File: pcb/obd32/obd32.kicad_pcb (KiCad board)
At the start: 2 copper layers, 43.2 x 43.2 mm, 36 parts, among them J1 USB_C_Receptacle_USB2.0, J2 Micro_SD_Card, J3 Conn_02x08_Top_Bottom, J4 USB_A, U1 LMR33630ADDA, U2 CP2102N-A01-GQFN24, U3 AP1117-33, U4 ESP32-WROOM-32, U5 SiP32431DR3, U6 MCP2562-E-MF

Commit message: Maybe version of board
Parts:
- removed C7, C8: 22µF, Capacitor_SMD:C_0805_2012Metric
- added C15: 10nF, Capacitor_SMD:C_0201_0603Metric, B.Cu at (236.2, 73.7)
- added C16: 0.47µF, Capacitor_SMD:C_0201_0603Metric, B.Cu at (236.7, 74.4)
- added C17: 0.1µF, Capacitor_SMD:C_0201_0603Metric, B.Cu at (238.8, 74.4)
- added C18: 0.1µF, Capacitor_SMD:C_0201_0603Metric, B.Cu at (229.6, 83.8)
- added D3: LED, LED_SMD:LED_0402_1005Metric, F.Cu at (221.0, 91.2)
- added D4: LED, LED_SMD:LED_0402_1005Metric, F.Cu at (223.3, 91.2)
- added D5: LED, LED_SMD:LED_0402_1005Metric, F.Cu at (225.6, 91.2)
- added J5: Conn_01x04_Female, Connector_PinSocket_2.54mm:PinSocket_1x04_P2.54mm_Vertical_SMD_Pin1Left, F.Cu at (199.9, 80.5)
- added R10: 4K7, Resistor_SMD:R_0201_0603Metric, F.Cu at (236.2, 90.4)
- added R11: 4K7, Resistor_SMD:R_0201_0603Metric, F.Cu at (237.5, 90.4)
- added R12: 65R, Resistor_SMD:R_0201_0603Metric, F.Cu at (222.5, 90.2)
- added R13: 65R, Resistor_SMD:R_0201_0603Metric, F.Cu at (224.0, 90.2)
- added R14: 5R, Resistor_SMD:R_0201_0603Metric, F.Cu at (225.6, 90.2)
- added SW1: SW_Push, Button_Switch_SMD:SW_SPST_B3U-3000P-B, F.Cu at (198.4, 64.8)
- added SW2: SW_Push, Button_Switch_SMD:SW_SPST_B3U-3000P-B, F.Cu at (198.4, 69.8)
- added U7: LPS25HB, Package_LGA:ST_HLGA-10_2.5x2.5mm_P0.6mm_LayoutBorder3x2y, B.Cu at (231.6, 84.1)
- C11, C12: value 100nF -> 0.1µF; footprint Capacitor_SMD:C_0805_2012Metric -> Capacitor_SMD:C_0201_0603Metric; moved to B.Cu
- C13, C14, C4: value 100nF -> 0.1µF; footprint Capacitor_SMD:C_0805_2012Metric -> Capacitor_SMD:C_0201_0603Metric
- C3: footprint Capacitor_SMD:C_0805_2012Metric -> Capacitor_SMD:C_0402_1005Metric
- C9: footprint Capacitor_SMD:C_0805_2012Metric -> Capacitor_SMD:C_0603_1608Metric
- J1: value USB_C_Receptacle_USB2.0 -> Conn_01x04_Male; footprint Connector_USB:USB_C_Receptacle_HRO_TYPE-C-31-M-12 -> Connector_Molex:Molex_PicoBlade_53048-0410_1x04_P1.25mm_Horizontal
- J3: value Conn_02x08_Top_Bottom -> OBD2; footprint Connector_PinHeader_2.54mm:PinHeader_2x08_P2.54mm_Vertical -> OBD2:OBD2
- J4: value USB_A -> 67329-8040; footprint Connector_USB:USB_A_Molex_105057_Vertical -> 67329-8040:673298040
- L1: value 8µH -> 2.2µH; footprint Inductor_SMD:L_Coilcraft_XxL4040 -> TDK_SPM5030:TDK_SPM5030
- R1, R2, R3, R4, R9: footprint Resistor_SMD:R_0603_1608Metric -> Resistor_SMD:R_0201_0603Metric
- R5, R6: value 5K1 -> 100K; footprint Resistor_SMD:R_0603_1608Metric -> Resistor_SMD:R_0201_0603Metric
- R7, R8: footprint Resistor_SMD:R_0603_1608Metric -> Resistor_SMD:R_0201_0603Metric; moved to F.Cu
- U1: value LMR33630ADDA -> LMR33630BDDA
- U2: value CP2102N-A01-GQFN24 -> ICM-20689; footprint Package_DFN_QFN:QFN-24-1EP_4x4mm_P0.5mm_EP2.6x2.6mm -> ICM-20689:QFN50P400X400X95-25N-D; moved to B.Cu
- U5: moved to B.Cu
- moved R5 38.9 mm to (237.2, 69.8), turned to 0 degrees
- moved J4 35.8 mm to (199.0, 103.6), turned to 90 degrees
- moved R6 35.2 mm to (226.8, 69.6), turned to 0 degrees
- moved J3 32.6 mm to (235.7, 64.1), turned to 180 degrees
- moved U2 32.3 mm to (236.5, 77.5)
- moved C12 24.0 mm to (209.8, 107.7)
- moved U5 21.3 mm to (209.4, 105.7), turned to 90 degrees
- moved R8 20.8 mm to (215.4, 73.8), turned to 270 degrees
- moved C11 19.6 mm to (209.0, 103.6)
- moved R7 17.7 mm to (215.4, 72.2), turned to 270 degrees
- moved C10 16.9 mm to (207.6, 90.4)
- moved C9 16.9 mm to (207.6, 86.6)
- moved U3 16.9 mm to (202.0, 88.5)
- moved C1 15.6 mm to (213.9, 73.2), turned to 270 degrees
- moved R1 14.1 mm to (207.8, 70.4), turned to 180 degrees
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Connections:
- J2 pad 9: Earth -> GND
- R5 pad 1: GND -> ESP32_EN
- R5 pad 2: Net-(J1-PadA5) -> +3V3
- R6 pad 1: Net-(J1-PadB5) -> ESP32_MISC
- R6 pad 2: GND -> +3V3
- U2 pad 10: (no net) -> Net-(C16-Pad2)
- U2 pad 12: (no net) -> IMU_INT
- U2 pad 13: (no net) -> +3V3
- U2 pad 2: GND -> (no net)
- U2 pad 20: UART_TX -> (no net)
- U2 pad 21: UART_RX -> (no net)
- U2 pad 22: (no net) -> +3V3
- U2 pad 23: (no net) -> I2C0_SCL
- U2 pad 24: (no net) -> I2C0_SDA
- U2 pad 3: USB_D+ -> (no net)
- U2 pad 4: USB_D- -> (no net)
- U2 pad 7: +5VA -> (no net)
- U2 pad 8: +5VA -> +3V3
- U2 pad 9: (no net) -> GND
- U4 pad 11: (no net) -> ESP32_MISC
- U4 pad 12: (no net) -> CAN_SHDN
- U4 pad 13: (no net) -> CAN_RX
- U4 pad 14: (no net) -> CAN_TX
- U4 pad 23: (no net) -> GPS_RX
- U4 pad 24: (no net) -> GPS_TX
- U4 pad 26: CAN_TX -> LED_R
- U4 pad 27: CAN_SHDN -> LED_G
- U4 pad 28: (no net) -> LED_B
- U4 pad 29: CAN_RX -> (no net)
- U4 pad 3: +3V3 -> ESP32_EN
- U4 pad 30: (no net) -> USB_EN
- U4 pad 31: (no net) -> BARO_INT
- U4 pad 36: (no net) -> I2C0_SDA
- U4 pad 37: (no net) -> I2C0_SCL
- U4 pad 7: USB_EN -> IMU_INT
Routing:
- net GND: track 203.4 -> 351.0 mm, vias 2 -> 8
- net +3V3: track 71.9 -> 171.7 mm, vias 3 -> 5
- net Earth: track 78.5 -> 0.00 mm
- net +BATT: track 61.8 -> 13.7 mm
- net ESP32_EN: track 0.00 -> 45.5 mm
- net ESP32_MISC: track 0.00 -> 34.6 mm, vias 0 -> 2
- net GPS_RX: track 0.00 -> 24.4 mm, vias 0 -> 2
- net GPS_TX: track 0.00 -> 24.3 mm, vias 0 -> 2
- net I2C0_SCL: track 0.00 -> 19.7 mm, vias 0 -> 2
- net Net-(R7-Pad2): track 4.93 -> 23.9 mm, vias 1 -> 0
- net CAN_H: track 27.3 -> 8.47 mm
- net +5VA: track 23.7 -> 6.21 mm, vias 2 -> 0
- net I2C0_SDA: track 0.00 -> 15.9 mm, vias 0 -> 1
- net +5V: track 44.6 -> 58.0 mm, vias 3 -> 2
- net Net-(C5-Pad1): track 23.2 -> 12.5 mm
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- added copper zone on B.Cu, net GND
- added copper zone on F.Cu, net GND
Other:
- board size 43.2 x 43.2 mm -> 49.5 x 48.8 mm
- board text added: "5V 3A"
- board text added: "GPS"
- board text added: "UART"
- board text removed: "5V 3A DC-DC"

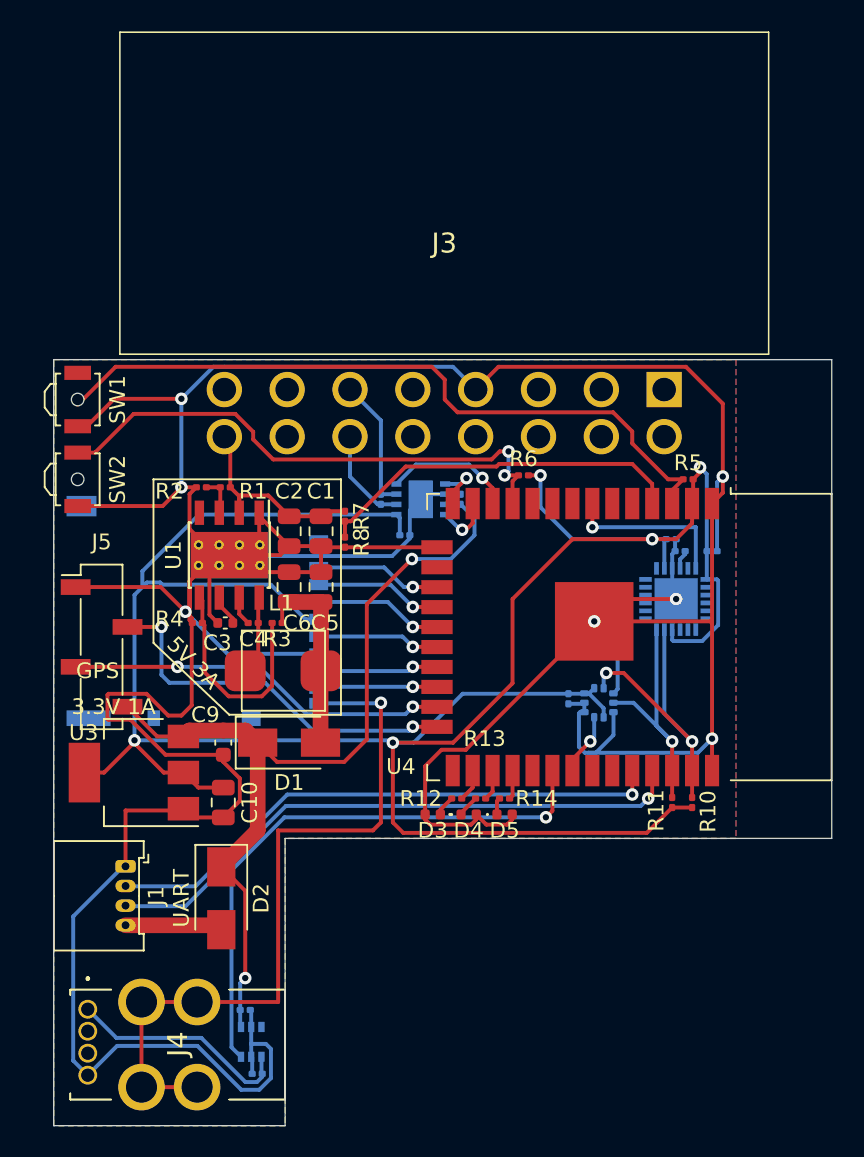
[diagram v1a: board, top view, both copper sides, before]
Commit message: Board: Add USB-C and CP2102 UART converter
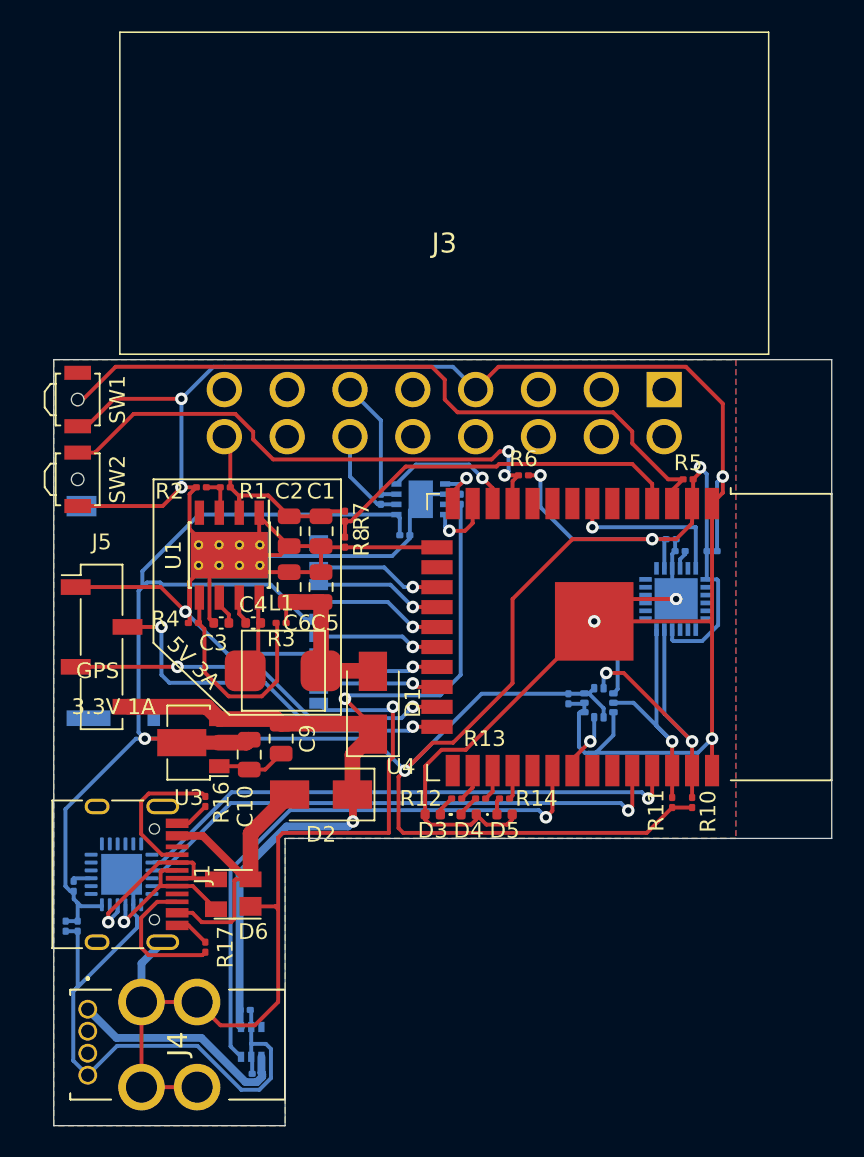
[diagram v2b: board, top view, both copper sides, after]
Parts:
- added C7: 4.7µF, Capacitor_SMD:C_0201_0603Metric, B.Cu at (197.6, 98.3)
- added C8: 0.1µF, Capacitor_SMD:C_0201_0603Metric, B.Cu at (198.4, 98.3)
- added D6: SP0503BAHT, Package_TO_SOT_SMD:SOT-143, F.Cu at (208.3, 96.3)
- added R15: 1K, Resistor_SMD:R_0201_0603Metric, B.Cu at (198.1, 95.8)
- added R16: 5.1K, Resistor_SMD:R_0201_0603Metric, F.Cu at (206.5, 90.4)
- added R17: 5.1K, Resistor_SMD:R_0201_0603Metric, F.Cu at (206.5, 99.6)
- added U8: CP2102N-A01-GQFN24, Package_DFN_QFN:QFN-24-1EP_4x4mm_P0.5mm_EP2.6x2.6mm, B.Cu at (201.2, 95.0)
- C4: footprint Capacitor_SMD:C_0201_0603Metric -> Capacitor_SMD:C_0402_1005Metric
- C9: footprint Capacitor_SMD:C_0603_1608Metric -> Capacitor_SMD:C_0805_2012Metric
- J1: value Conn_01x04_Male -> USB_C_Receptacle_USB2.0; footprint Connector_Molex:Molex_PicoBlade_53048-0410_1x04_P1.25mm_Horizontal -> Connector_USB:USB_C_Receptacle_HRO_TYPE-C-31-M-12
- U3: value AP1117-33 -> AZ1117C-3.3; footprint Package_TO_SOT_SMD:SOT-223-3_TabPin2 -> Package_TO_SOT_SMD:SOT-89-3
- moved D2 9.16 mm to (213.9, 89.9), turned to 180 degrees
- moved D1 5.91 mm to (217.2, 84.1), turned to 90 degrees
- moved U3 4.24 mm to (205.7, 86.6)
- moved C9 3.69 mm to (211.3, 86.4)
- moved C10 3.47 mm to (209.3, 87.4)
- moved J1 0.92 mm to (200.7, 95.0)
- moved C3 0.25 mm to (207.5, 79.0)
- moved R3 0.25 mm to (211.3, 79.0)
- moved R4 0.25 mm to (205.7, 79.0)
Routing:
- net GND: track 351.0 -> 336.3 mm
- net +5VA: track 6.21 -> 19.7 mm
- net USB_D-: track 0.00 -> 13.2 mm, vias 0 -> 1
- net +3V3: track 171.7 -> 183.4 mm
- net USB_D+: track 0.00 -> 11.5 mm, vias 0 -> 1
- net Net-(J1-PadA5): track 0.00 -> 9.30 mm
- net Net-(J1-PadB5): track 0.00 -> 8.97 mm
- net +5V: track 58.0 -> 64.8 mm
- net UART_TX: track 38.0 -> 35.4 mm
- net Net-(C5-Pad1): track 12.5 -> 11.1 mm
- net UART_RX: track 36.2 -> 34.8 mm
- net Net-(R15-Pad2): track 0.00 -> 1.27 mm
- net CAN_RX: track 3.58 -> 4.08 mm
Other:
- board text removed: "UART"

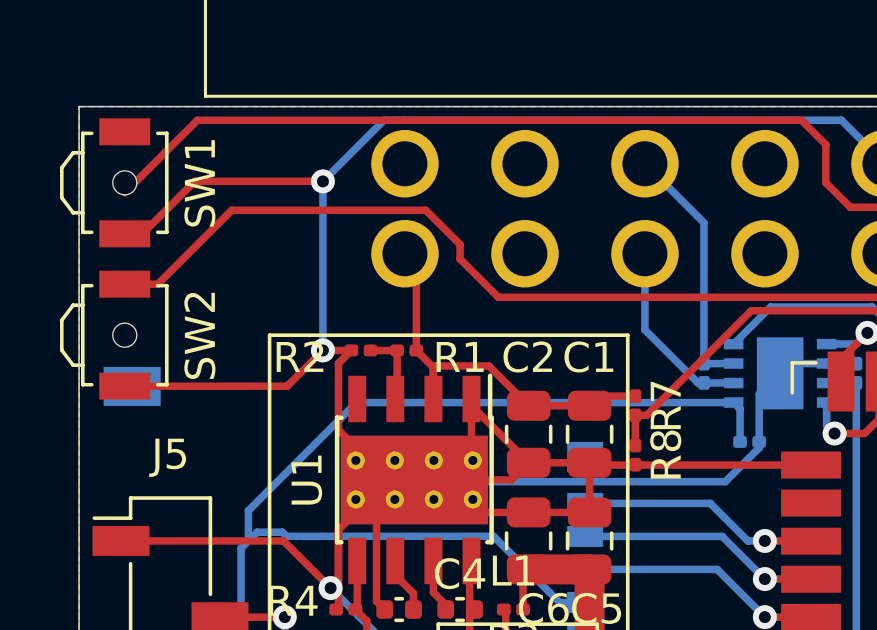
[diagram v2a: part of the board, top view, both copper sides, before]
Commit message: Board: Add cuttable solder jumper to allow disconnection from 12V rail
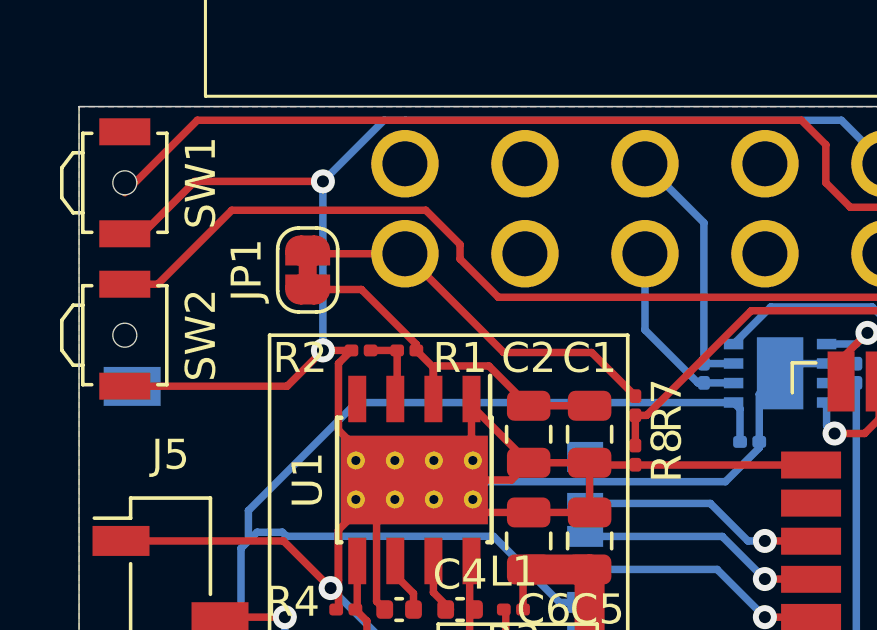
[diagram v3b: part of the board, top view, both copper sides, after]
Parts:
- added JP1: SolderJumper_2_Bridged, Jumper:SolderJumper-2_P1.3mm_Bridged_RoundedPad1.0x1.5mm, F.Cu at (204.5, 67.7)
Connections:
- C1 pad 1: +BATT -> Net-(C1-Pad1)
- C2 pad 2: +BATT -> Net-(C1-Pad1)
- R1 pad 1: +BATT -> Net-(C1-Pad1)
- U1 pad 2: +BATT -> Net-(C1-Pad1)
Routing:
- net Net-(C1-Pad1): track 0.00 -> 13.2 mm
- net +BATT: track 13.7 -> 12.9 mm

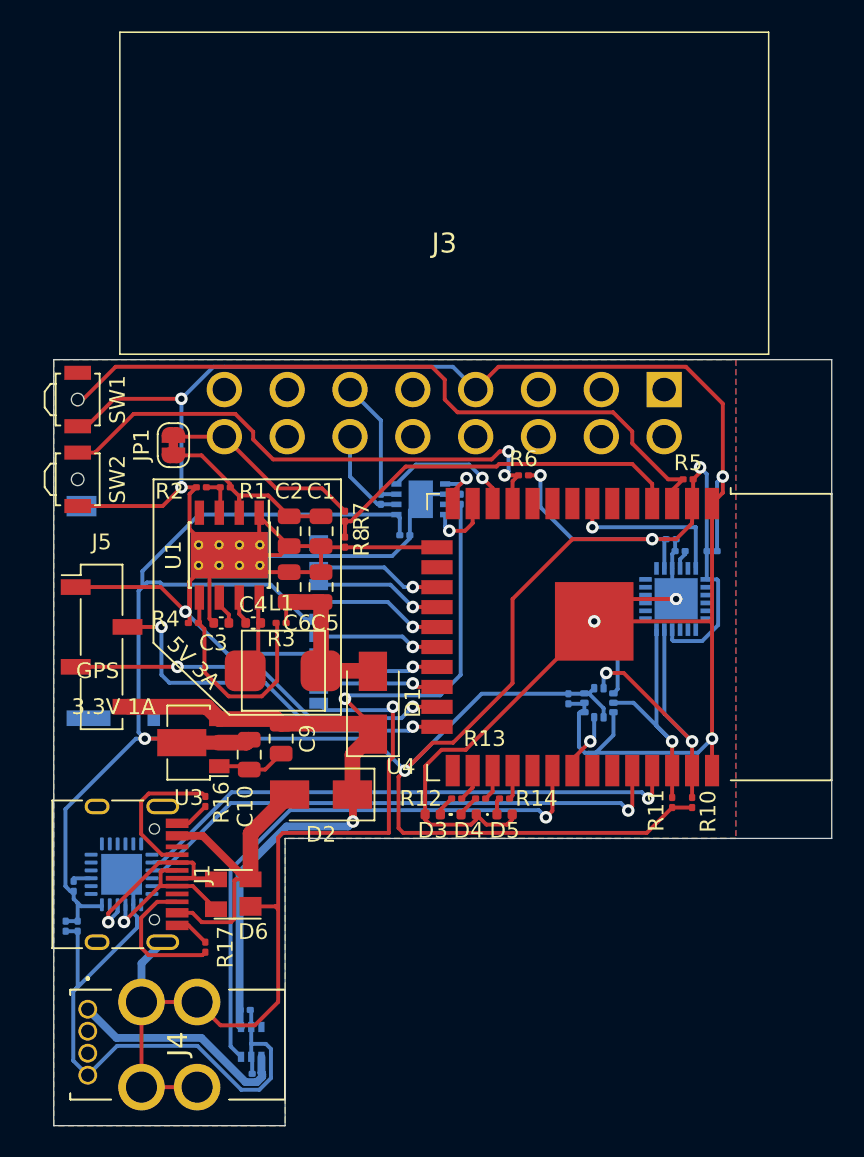
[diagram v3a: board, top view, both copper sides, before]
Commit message: Board: replace pressure sensor with more common bmp280
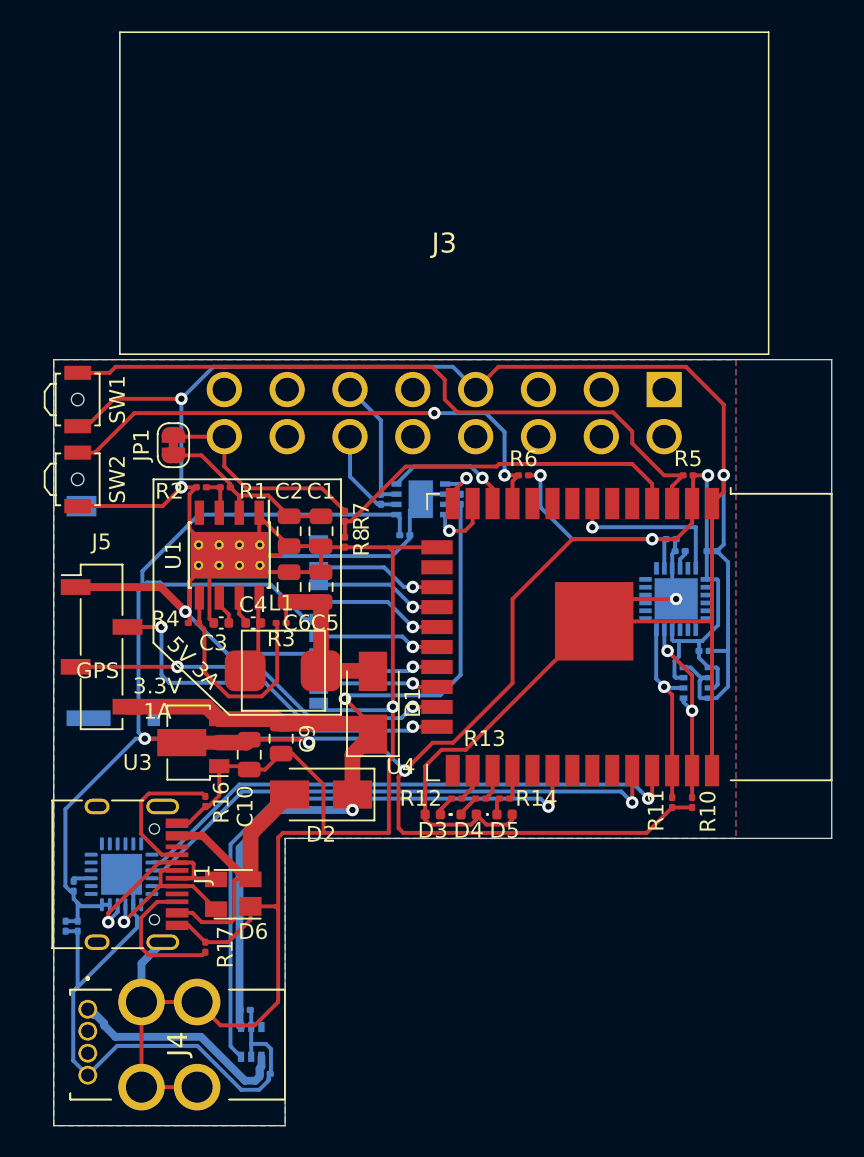
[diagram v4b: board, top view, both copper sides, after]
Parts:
- U7: value LPS25HB -> BMP280; footprint Package_LGA:ST_HLGA-10_2.5x2.5mm_P0.6mm_LayoutBorder3x2y -> Package_LGA:Bosch_LGA-8_2x2.5mm_P0.65mm_ClockwisePinNumbering
- moved C18 9.16 mm to (238.3, 80.8), turned to 180 degrees
- moved U7 6.32 mm to (237.7, 82.8)
- moved C12 0.51 mm to (210.3, 107.7), turned to 0 degrees
- moved R5 0.25 mm to (237.2, 69.6)
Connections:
- U4 pad 31: BARO_INT -> (no net)
- U7 pad 1: +3V3 -> GND
- U7 pad 2: I2C0_SCL -> +3V3
- U7 pad 3: GND -> I2C0_SDA
- U7 pad 4: I2C0_SDA -> I2C0_SCL
- U7 pad 7: BARO_INT -> GND
- U7 pad 8: GND -> +3V3
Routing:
- net GND: track 336.3 -> 353.4 mm, vias 8 -> 6
- net I2C0_SCL: track 19.7 -> 12.4 mm
- net +3V3: track 183.4 -> 178.8 mm, vias 5 -> 6
- net BARO_INT: track 3.97 -> 0.00 mm, vias 1 -> 0
- net I2C0_SDA: track 15.9 -> 12.4 mm
- net +BATT: track 12.9 -> 14.0 mm
- net ESP32_EN: track 45.5 -> 44.8 mm
- net USB_EN: track 37.2 -> 37.8 mm
